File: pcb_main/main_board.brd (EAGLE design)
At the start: 82 x 81.2 mm, 54 parts, among them Q1 FDS5680, T1 BC847, U1 STM32F411RET6, X1 FH12-14S-0.5SH

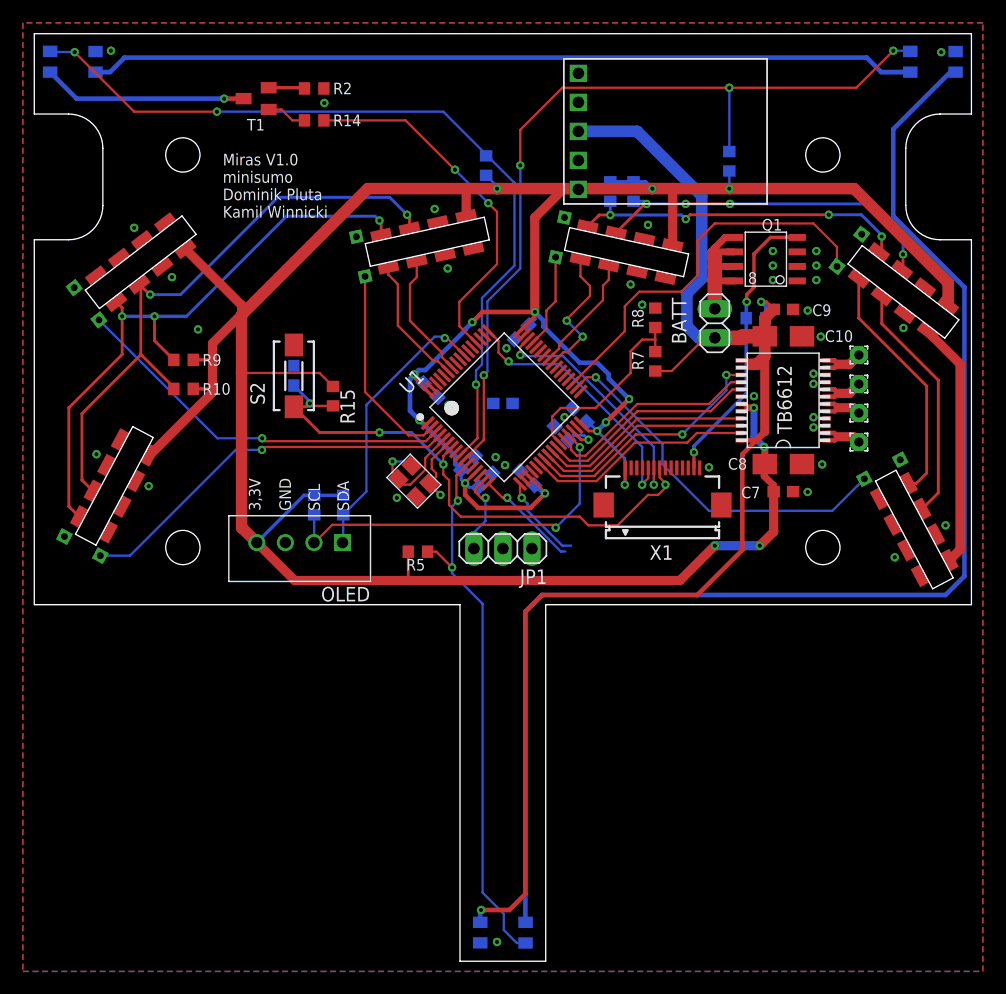
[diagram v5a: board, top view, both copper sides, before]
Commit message: 2 h-bridges, 5V reg
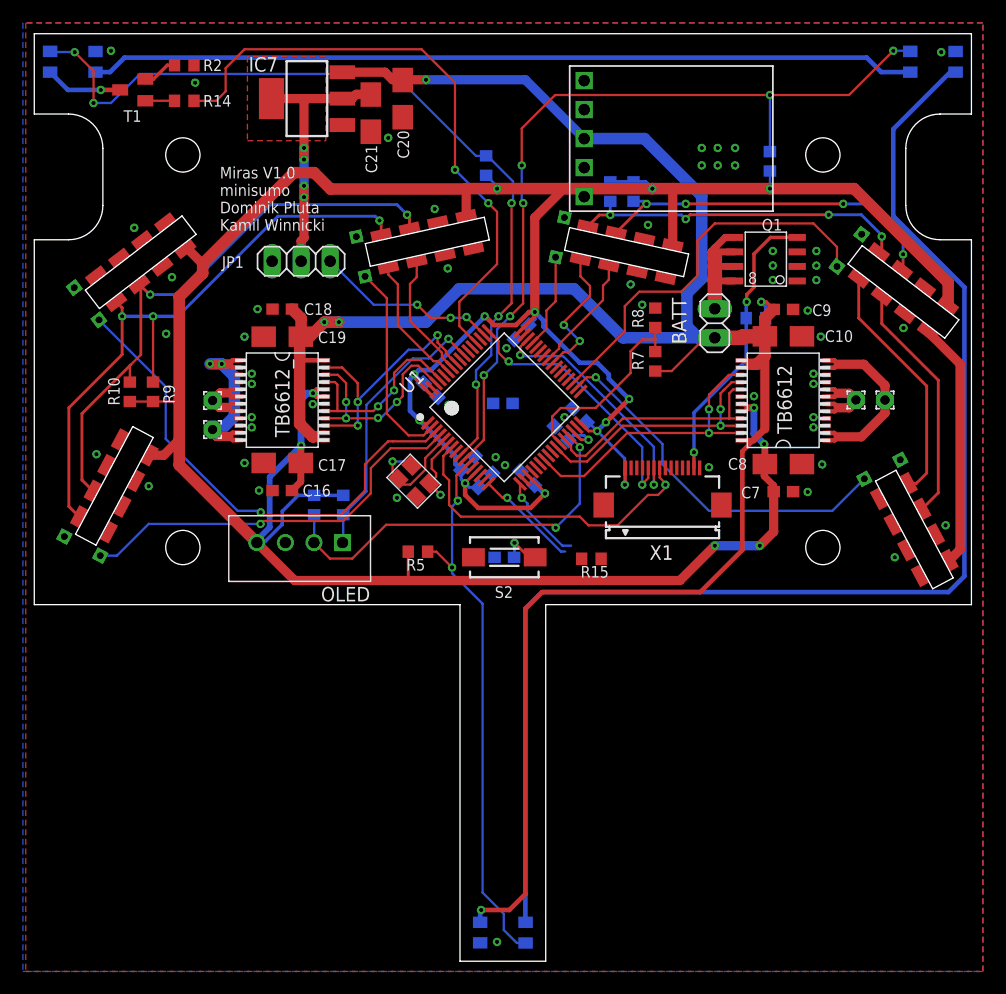
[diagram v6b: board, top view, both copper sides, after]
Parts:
- removed H1, H2: (no value), wirepad:1,6/0,8
- added C16, C18: 100n, rcl:C0603
- added C17, C19, C20, C21: 10u, rcl:B/3528-21W
- added H5, H6: (no value), wirepad:1,6/0,8
- added IC7: LM1117IMPX-5.0, lm1117:SOT223
- added TB6612_: TB6612FNG, tb6612:SSOP24
- moved JP1 30.7 mm to (-17.7, 25.1), turned to 0 degrees
- moved R15 26.7 mm to (7.75, -0.89), turned to 180 degrees
- moved C15 24.3 mm to (0.13, -0.76), turned to 0 degrees
- moved S2 24.3 mm to (0.13, -0.76), turned to 180 degrees
- moved R2 11.5 mm to (-27.9, 42.3)
- moved R14 11.5 mm to (-27.9, 39.2)
- moved T1 10.8 mm to (-32.4, 40.1)
- moved R10 4.71 mm to (-32.6, 13.7), turned to 270 degrees
- moved H3 4.55 mm to (33.4, 13.0)
- moved R9 3.86 mm to (-30.6, 13.7), turned to 270 degrees
- moved R4 3.56 mm to (23.4, 33.9)
- moved H4 1.42 mm to (30.9, 13.0)
- moved U$7 0.81 mm to (5.84, 42.2)
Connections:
- removed net AO: H1.1, TB6612.1, TB6612.2
- removed net AO2: H2.1, TB6612.5, TB6612.6
- removed net A_DIR_1: TB6612.21, U1.25
- removed net A_DIR_2: TB6612.22, U1.24
- removed net B_DIR_1: TB6612.17, U1.26
- removed net B_DIR_2: TB6612.16, U1.28
- removed net N$7: U1.57
- removed net PWMA: TB6612.23, U1.22
- removed net PWMB: TB6612.15, U1.23
- removed net VCC: JP1.2
- new net +5V: C21.+, IC7.2, IC7.TAB, JP1.2
- new net BO3: H5.1, TB6612_.1, TB6612_.11, TB6612_.12, TB6612_.2
- new net BO4: H6.1, TB6612_.5, TB6612_.6, TB6612_.7, TB6612_.8
- new net L_DIR_1: TB6612_.17, TB6612_.21, U1.61
- new net L_DIR_2: TB6612_.16, TB6612_.22, U1.62
- new net L_PWM: TB6612_.15, TB6612_.23, U1.57
- new net R_DIR_1: TB6612.17, TB6612.21, U1.28
- new net R_DIR_2: TB6612.16, TB6612.22, U1.26
- new net R_PWM: TB6612.15, TB6612.23, U1.23
- net 3,3V: now also C16.1, C17.+, TB6612_.19, TB6612_.20
- net BAT+: now also C18.1, C19.+, C20.+, IC7.3, TB6612_.13, TB6612_.14, TB6612_.24
- net BO1: now also TB6612.1, TB6612.2
- net BO2: now also TB6612.5, TB6612.6
- net GND: now also C16.2, C17.-, C18.2, C19.-, C20.-, C21.-, IC7.1, TB6612_.10, TB6612_.18, TB6612_.3, TB6612_.4, TB6612_.9
- net SERVO: now also U1.50; no longer U1.15
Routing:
- net BAT+: track 120.7 -> 201.4 mm, vias 2 -> 5
- net R_PWM: track 0.00 -> 26.0 mm, vias 0 -> 2
- net +5V: track 0.00 -> 25.2 mm, vias 0 -> 4
- net R_DIR_2: track 0.00 -> 22.8 mm, vias 0 -> 2
- net L_PWM: track 0.00 -> 22.5 mm, vias 0 -> 3
- net PWMB: track 22.2 -> 0.00 mm, vias 2 -> 0
- net LS_ON: track 31.9 -> 53.4 mm
- net R_DIR_1: track 0.00 -> 20.7 mm
- net PWMA: track 19.8 -> 0.00 mm
- net B_DIR_1: track 19.1 -> 0.00 mm
- net A_DIR_2: track 18.9 -> 0.00 mm
- net B_DIR_2: track 18.8 -> 0.00 mm
- net A_DIR_1: track 18.6 -> 0.00 mm
- net L_DIR_2: track 0.00 -> 18.5 mm, vias 0 -> 4
- net RST: track 49.5 -> 32.2 mm, vias 4 -> 2
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- added copper zone on layer 1, net +5V

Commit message: almost done
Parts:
- moved H3 3.78 mm to (30.6, 10.5)
- moved R15 2.16 mm to (5.84, -1.91), turned to 90 degrees
- moved H4 0.25 mm to (30.6, 13.0)
- moved C21 0.25 mm to (-11.3, 38.1)
- moved C20 0.13 mm to (-8.64, 39.4)
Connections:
- net R_PWM: now also U1.22; no longer U1.23
- net X6: now also U1.25; no longer U1.34
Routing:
- net RST: track 32.2 -> 37.6 mm, vias 2 -> 3
- net LS1: track 75.3 -> 73.3 mm
- net X6: track 32.6 -> 30.8 mm, vias 1 -> 4
- net BO1: track 16.8 -> 15.7 mm, vias 0 -> 2
- net BAT+: track 201.4 -> 200.8 mm
- net BO2: track 8.22 -> 7.71 mm
- net SERVO: vias 3 -> 4
- net GND: vias 55 -> 59

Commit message: main pcb done
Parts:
- added LED1, LED2: (no value), led:CHIPLED_0603
- added R16: 1k?, rcl:R0603
- added R17: 470R?, rcl:R0603
- R15: value 130R -> 10k
- R3, R4, R5: value (none) -> 4k7
- R7: value (none) -> 33k?
- R8: value (none) -> 10k
- moved C14 5.27 mm to (-4.65, 10.2), turned to 135 degrees
- moved X1 2.29 mm to (14.1, 1.52)
- moved R5 1.96 mm to (-6.46, -1.97), turned to 270 degrees
- moved R15 0.51 mm to (5.33, -1.91)
- moved C20 0.25 mm to (-8.38, 39.4)
- moved C18 0.13 mm to (-19.3, 21.1)
- moved C17 0.13 mm to (-19.3, 7.37)
- moved C16 0.13 mm to (-19.3, 4.95)
- moved C19 0.13 mm to (-19.3, 18.7)
- renumbered JP1 to SERVO
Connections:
- removed net +5V: C21.+, IC7.2, IC7.TAB, SERVO.2
- new net 5V: C21.+, IC7.2, IC7.TAB, LED1.A, SERVO.2
- new net N$1: LED1.C, R16.1
- new net N$7: LED2.C, R17.1
- new net STARTER: U1.33, X1.2
- net 3,3V: now also LED2.A
- net GND: now also R16.2, R17.2
- net LED: now also U1.34
- net RX: now also X1.3
- net SW1: now also U1.24
- net SW2: now also U1.23
- net SW3: now also U1.21
- net SW4: now also U1.20
- net TX: now also X1.4
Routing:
- net 5V: track 0.00 -> 27.8 mm, vias 0 -> 4
- net +5V: track 25.4 -> 0.00 mm, vias 4 -> 0
- net STARTER: track 0.00 -> 17.1 mm, vias 0 -> 2
- net SW1: track 0.00 -> 15.9 mm
- net SW3: track 0.00 -> 15.9 mm
- net LED: track 0.00 -> 15.6 mm, vias 0 -> 2
- net SW2: track 0.00 -> 15.6 mm
- net SW4: track 0.00 -> 15.6 mm
- net TX: track 9.18 -> 21.0 mm, vias 1 -> 2
- net RX: track 7.72 -> 18.1 mm, vias 1 -> 2
- net 3,3V: track 332.5 -> 339.6 mm, vias 19 -> 18
- net SWCLK: track 23.2 -> 28.5 mm
- net X6: track 30.8 -> 35.6 mm
- net N$7: track 0.00 -> 2.92 mm, vias 0 -> 1
- net ROBOT_OFF: track 25.3 -> 28.1 mm
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- added copper zone on layer 1, net 5V
- removed copper zone on layer 1, net +5V
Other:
- board text added: "5V"
- board text added: "PWM"
